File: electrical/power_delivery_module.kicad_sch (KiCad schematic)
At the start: 8 parts, among them U2 UA78L05AI

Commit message: Work in progress
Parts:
- added C4: 15n, symbol Device:C
- C1: value 200n -> 100n
- R1: value 10k -> 100k; Tolerance (none) -> 1%
- R6: value 20k -> 200k; Tolerance (none) -> 1%
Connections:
- net GND: now also C4.2
- net POWER_12: no longer R6.1
- net POWER_SENSE: now also C4.1
- net at D8.2 (A), F3.2, J?.1 (Pin_1): now also R6.1
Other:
- moved on the sheet: C1, C2, D8, F3, J?, R1, R6, U2

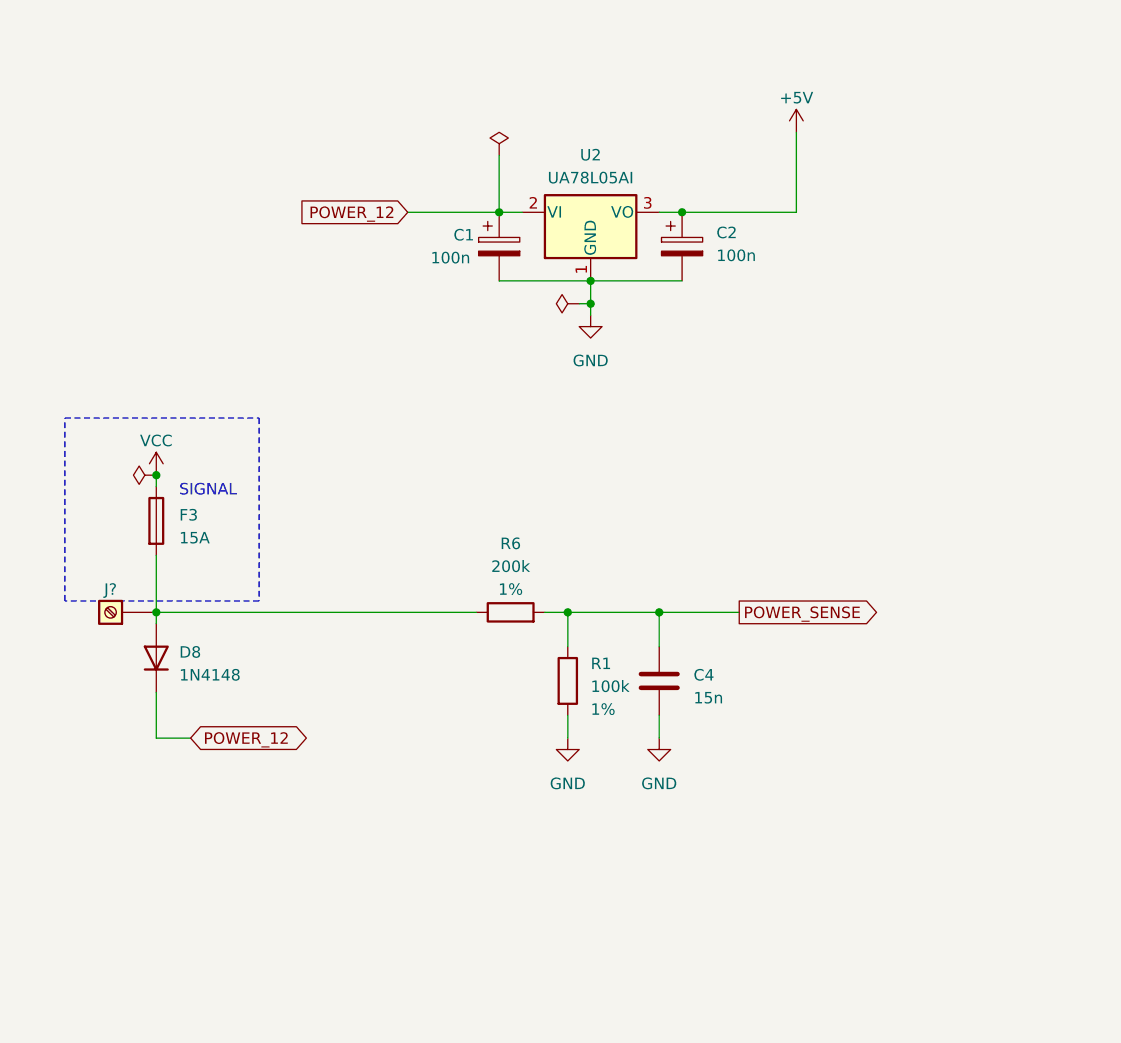
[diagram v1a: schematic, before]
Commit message: Aktualizacja KiCad i schematu - LED do debugowania
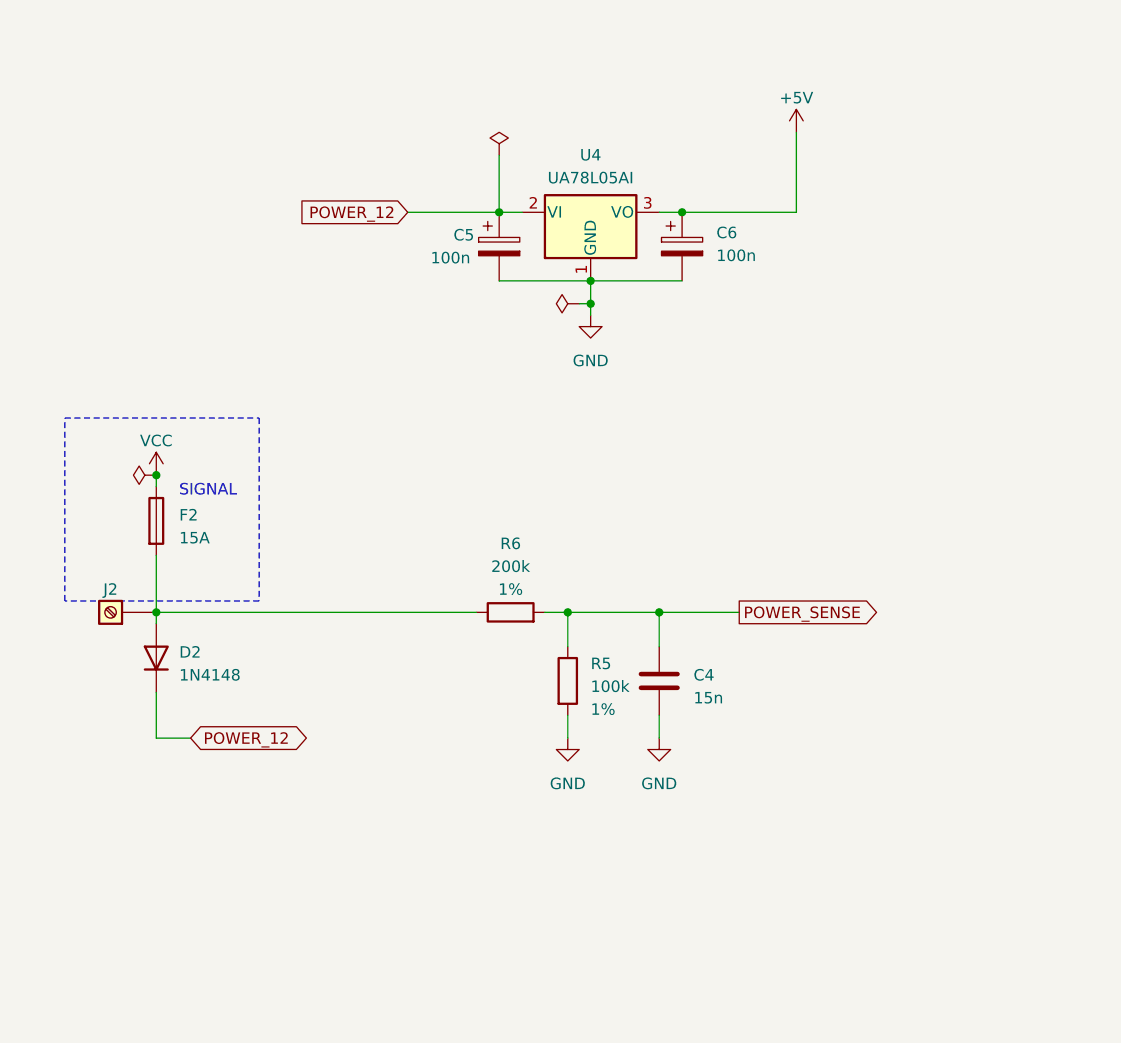
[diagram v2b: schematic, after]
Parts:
- gave numbers to parts that had none: 1
- renumbered C1 to C5, C2 to C6, D8 to D2, F3 to F2, R1 to R5, U2 to U4

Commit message: Względenie działa
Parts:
- removed C4: 15n, symbol Device:C
- removed R5: 100k, symbol Device:R
- removed R6: 200k, symbol Device:R
- added D8: 1N4148, Diode_THT:D_DO-41_SOD81_P10.16mm_Horizontal, symbol Diode:1N4002
- added J4: Screw_Terminal_01x01, symbol Connector:Screw_Terminal_01x01
- added R12: 10, symbol Device:R
- added R17: 75, symbol Device:R
- C5: value 100n -> 1u
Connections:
- net GND: now also J4.1 (Pin_1), R12.1
- net POWER_12: no longer names the net of C5.1, U4.2 (VI)
- net POWER_12: now also R17.2; no longer D2.1 (K)
- new net: D2.1 (K), D8.1 (K), R17.1
- new net AGND: R12.2
- new net BULB_POWER_12: D8.2 (A)
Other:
- moved on the sheet: C5, C6, D2, F2, J2, U4
